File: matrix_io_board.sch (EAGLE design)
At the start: 114 parts, among them IC1 6N138, IC2 SN74LVC2G14, IC3 LM27675M5_CHARGEPUMP, IC4 LM324D, IC5 MCP4728_QUAD_DAC, IC6 4504D, IC7 SP34063A_BOOST_REG, IC8 FDS8958B

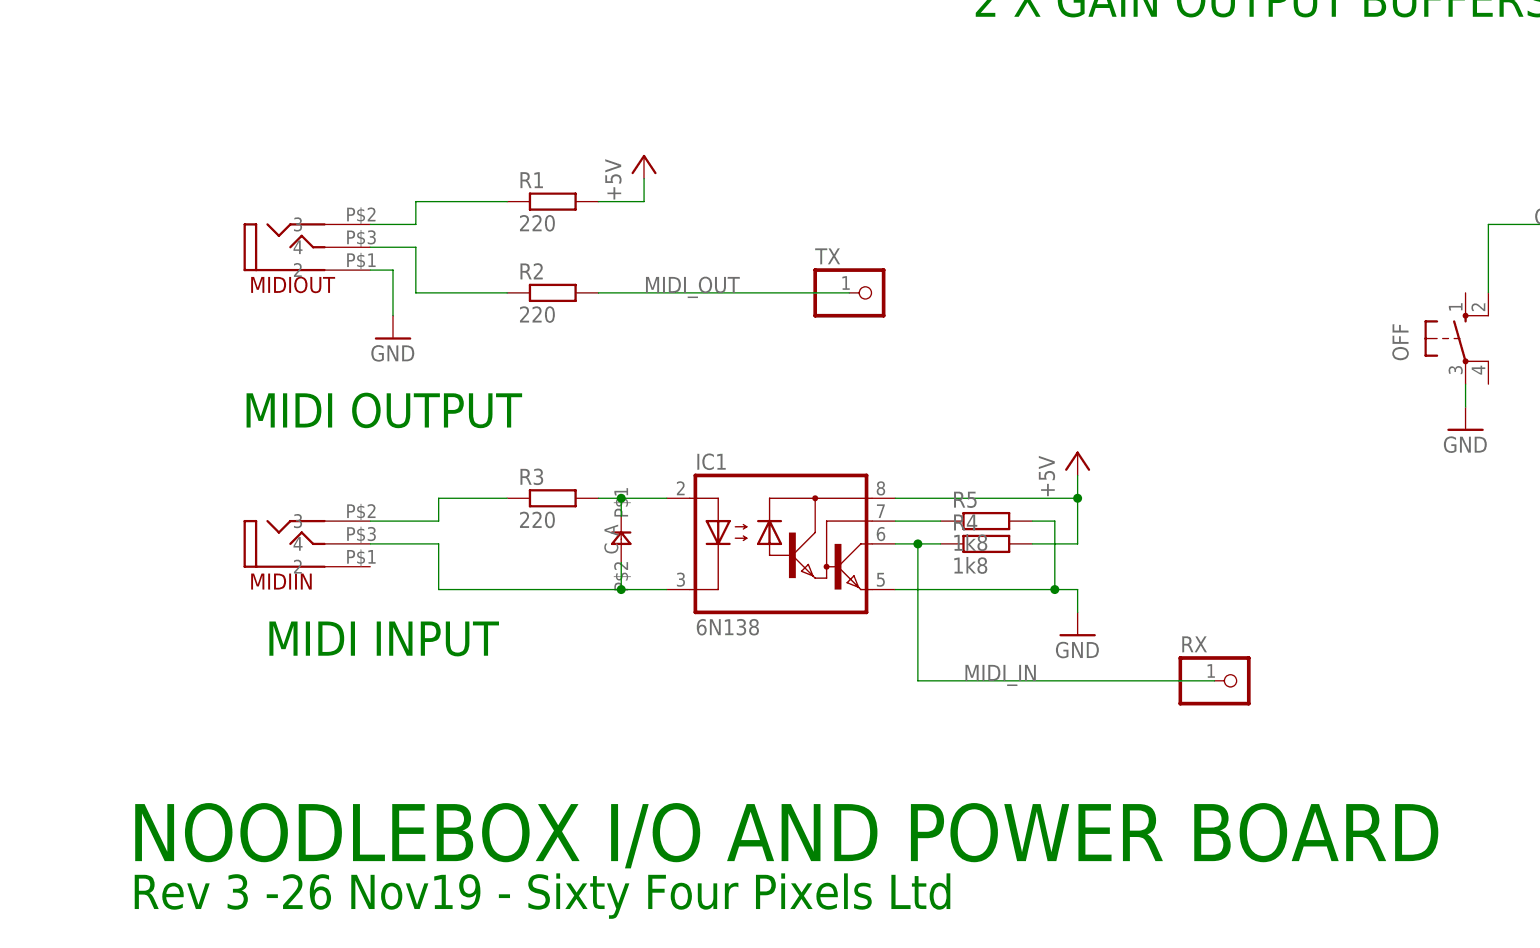
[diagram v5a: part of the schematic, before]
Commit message: use the new stereo Thonk sockets
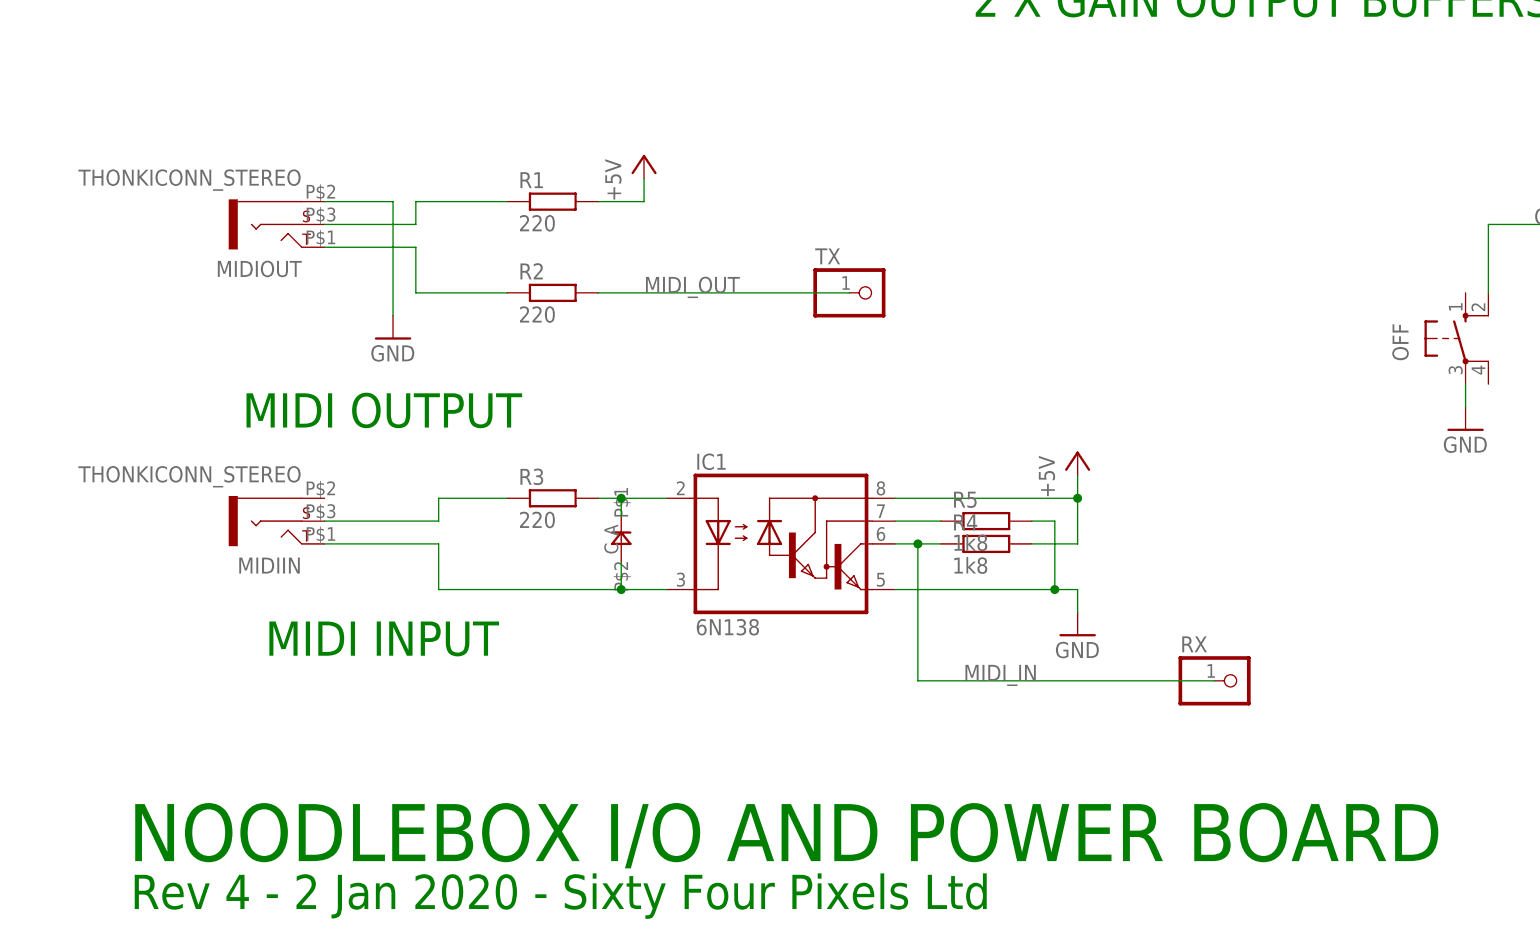
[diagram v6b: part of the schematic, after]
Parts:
- MIDIIN, MIDIOUT: value VERTICAL_3_5MM_SOCKETASSS -> THONKICONN_STEREO; device jason_eagle6:VERTICAL_3_5MM_SOCKETASSS -> jason_eagle6:THONKICONN_STEREO
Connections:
- net GND: now also MIDIOUT.R; no longer MIDIOUT.2
- net N$1: now also MIDIOUT.S; no longer MIDIOUT.3
- net N$4: now also MIDIIN.T; no longer MIDIIN.4
- net N$6: now also MIDIOUT.T; no longer MIDIOUT.4
- net N$7: now also MIDIIN.S; no longer MIDIIN.3
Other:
- note added: "Rev 4 - 2 Jan 2020 - Sixty Four Pixels Ltd"
- note removed: "Rev 3 -26 Nov19 - Sixty Four Pixels Ltd"
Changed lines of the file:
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@@
 <part name="C10" library="rcl" deviceset="C-EU" device="C0805" value="100n"/>
 <part name="GND29" library="supply1" deviceset="GND" device=""/>
-<part name="MIDIOUT" library="jason_eagle6" deviceset="VERTICAL_3_5MM_SOCKET" device="ASSS" value="VERTICAL_3_5MM_SOCKETASSS"/>
-<part name="MIDIIN" library="jason_eagle6" deviceset="VERTICAL_3_5MM_SOCKET" device="ASSS" value="VERTICAL_3_5MM_SOCKETASSS"/>
 <part name="CKO" library="thonkiconn" deviceset="WQP-PJ301M-12_JACK" device=""/>
 <part name="GT2" library="thonkiconn" deviceset="WQP-PJ301M-12_JACK" device=""/>
@@
 <part name="GD3" library="pinhead" deviceset="PINHD-1X1" device=""/>
 <part name="GD4" library="pinhead" deviceset="PINHD-1X1" device=""/>
+<part name="MIDIOUT" library="jason_eagle6" deviceset="THONKICONN_STEREO" device=""/>
+<part name="MIDIIN" library="jason_eagle6" deviceset="THONKICONN_STEREO" device=""/>
 </parts>
 <sheets>
@@
 <text x="359.156" y="117.094" size="3.81" layer="91">CLOCK INPUT</text>
 <text x="105.156" y="99.314" size="6.35" layer="91">NOODLEBOX I/O AND POWER BOARD</text>
-<text x="105.41" y="93.98" size="3.81" layer="91">Rev 3 -26 Nov19 - Sixty Four Pixels Ltd</text>
+<text x="105.41" y="93.98" size="3.81" layer="91">Rev 4 - 2 Jan 2020 - Sixty Four Pixels Ltd</text>
 </plain>
 <instances>
@@
 <instance part="C10" gate="G$1" x="416.56" y="228.6" rot="R180"/>
 <instance part="GND29" gate="1" x="396.24" y="215.9"/>
-<instance part="MIDIOUT" gate="G$1" x="121.92" y="167.64" rot="MR180"/>
-<instance part="MIDIIN" gate="G$1" x="121.92" y="134.62" rot="MR180"/>
 <instance part="CKO" gate="G$1" x="444.5" y="251.46" rot="MR180"/>
 <instance part="GT2" gate="G$1" x="444.5" y="241.3" rot="MR180"/>
@@
 <instance part="GD3" gate="G$1" x="429.26" y="327.66"/>
 <instance part="GD4" gate="G$1" x="429.26" y="320.04"/>
+<instance part="MIDIOUT" gate="G$1" x="121.92" y="170.18" rot="R180"/>
+<instance part="MIDIIN" gate="G$1" x="121.92" y="137.16" rot="R180"/>
 </instances>
 <busses>
@@
 <wire x1="160.02" y1="132.588" x2="160.02" y2="129.54" width="0.1524" layer="91"/>
 <junction x="160.02" y="129.54"/>
-<pinref part="MIDIIN" gate="G$1" pin="4"/>
-<wire x1="132.08" y1="134.62" x2="139.7" y2="134.62" width="0.1524" layer="91"/>
 <wire x1="139.7" y1="134.62" x2="139.7" y2="129.54" width="0.1524" layer="91"/>
+<pinref part="MIDIIN" gate="G$1" pin="T"/>
+<wire x1="127" y1="134.62" x2="139.7" y2="134.62" width="0.1524" layer="91"/>
 </segment>
 </net>
@@
 </segment>
 <segment>
-<pinref part="MIDIOUT" gate="G$1" pin="2"/>
 <pinref part="GND40" gate="1" pin="GND"/>
-<wire x1="132.08" y1="165.1" x2="134.62" y2="165.1" width="0.1524" layer="91"/>
-<wire x1="134.62" y1="165.1" x2="134.62" y2="160.02" width="0.1524" layer="91"/>
+<pinref part="MIDIOUT" gate="G$1" pin="R"/>
+<wire x1="127" y1="172.72" x2="134.62" y2="172.72" width="0.1524" layer="91"/>
+<wire x1="134.62" y1="172.72" x2="134.62" y2="160.02" width="0.1524" layer="91"/>
 </segment>
 </net>
@@
 <wire x1="137.16" y1="162.56" x2="147.32" y2="162.56" width="0.1524" layer="91"/>
 <wire x1="137.16" y1="162.56" x2="137.16" y2="167.64" width="0.1524" layer="91"/>
-<pinref part="MIDIOUT" gate="G$1" pin="4"/>
-<wire x1="137.16" y1="167.64" x2="132.08" y2="167.64" width="0.1524" layer="91"/>
+<wire x1="137.16" y1="167.64" x2="127" y2="167.64" width="0.1524" layer="91"/>
+<pinref part="MIDIOUT" gate="G$1" pin="T"/>
 </segment>
 </net>
@@
 <wire x1="147.32" y1="139.7" x2="139.7" y2="139.7" width="0.1524" layer="91"/>
 <wire x1="139.7" y1="139.7" x2="139.7" y2="137.16" width="0.1524" layer="91"/>
-<pinref part="MIDIIN" gate="G$1" pin="3"/>
-<wire x1="139.7" y1="137.16" x2="132.08" y2="137.16" width="0.1524" layer="91"/>
+<pinref part="MIDIIN" gate="G$1" pin="S"/>
+<wire x1="127" y1="137.16" x2="139.7" y2="137.16" width="0.1524" layer="91"/>
 </segment>
 </net>
@@
 <segment>
 <pinref part="R1" gate="G$1" pin="1"/>
-<pinref part="MIDIOUT" gate="G$1" pin="3"/>
-<wire x1="132.08" y1="170.18" x2="137.16" y2="170.18" width="0.1524" layer="91"/>
+<wire x1="127" y1="170.18" x2="137.16" y2="170.18" width="0.1524" layer="91"/>
 <wire x1="137.16" y1="170.18" x2="137.16" y2="172.72" width="0.1524" layer="91"/>
 <wire x1="137.16" y1="172.72" x2="147.32" y2="172.72" width="0.1524" layer="91"/>
-</segment>
-</net>
+<pinref part="MIDIOUT" gate="G$1" pin="S"/>
+</segment>
+</net>

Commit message: V4 ready to go
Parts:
- renumbered BATT+ to BT+, BATT- to BT-
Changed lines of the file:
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@@
 <part name="GND41" library="supply1" deviceset="GND" device=""/>
 <part name="L2" library="jason_eagle6" deviceset="NB_IND" device=""/>
-<part name="BATT+" library="pinhead" deviceset="PINHD-1X1" device=""/>
-<part name="BATT-" library="pinhead" deviceset="PINHD-1X1" device=""/>
+<part name="BT+" library="pinhead" deviceset="PINHD-1X1" device=""/>
+<part name="BT-" library="pinhead" deviceset="PINHD-1X1" device=""/>
 <part name="C1" library="rcl" deviceset="C-EU" device="C0805" value="100n"/>
 <part name="P+13" library="supply1" deviceset="+5V" device=""/>
@@
 <instance part="GND41" gate="1" x="284.48" y="299.72"/>
 <instance part="L2" gate="G$1" x="259.08" y="330.2" rot="R90"/>
-<instance part="BATT+" gate="G$1" x="99.06" y="368.3" rot="R180"/>
-<instance part="BATT-" gate="G$1" x="99.06" y="360.68" rot="R180"/>
+<instance part="BT+" gate="G$1" x="99.06" y="368.3" rot="R180"/>
+<instance part="BT-" gate="G$1" x="99.06" y="360.68" rot="R180"/>
 <instance part="C1" gate="G$1" x="335.28" y="147.32"/>
 <instance part="P+13" gate="1" x="335.28" y="170.18"/>
@@
 <wire x1="109.22" y1="347.98" x2="111.76" y2="347.98" width="0.1524" layer="91"/>
 <wire x1="111.76" y1="347.98" x2="111.76" y2="340.36" width="0.1524" layer="91"/>
-<pinref part="BATT-" gate="G$1" pin="1"/>
+<pinref part="BT-" gate="G$1" pin="1"/>
 <wire x1="101.6" y1="360.68" x2="111.76" y2="360.68" width="0.1524" layer="91"/>
 <wire x1="111.76" y1="347.98" x2="111.76" y2="360.68" width="0.1524" layer="91"/>
@@
 <net name="N$16" class="0">
 <segment>
-<pinref part="BATT+" gate="G$1" pin="1"/>
+<pinref part="BT+" gate="G$1" pin="1"/>
 <wire x1="101.6" y1="368.3" x2="114.3" y2="368.3" width="0.1524" layer="91"/>
 <pinref part="DC" gate="G$1" pin="NC"/>

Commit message: V5 first cut
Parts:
- C10, C11, C12, C5, C6, C7: value 100n -> 10n
- C19, C20, C22: device rcl:CPOL-EUE2.5-7 -> rcl:CPOL-EUD
- D7: value CGRM4001-G -> MBR0520LT; device diode:CGRM4001-G -> diode:MBR0520LT
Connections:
- net GND: now also MIDIOUT.S; no longer MIDIOUT.R
- net N$1: now also MIDIOUT.R; no longer MIDIOUT.S
- net N$7: now also MIDIIN.R; no longer MIDIIN.S
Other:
- note added: "CC-NC-BY-SA Commercial Use Not Allowed"
- note added: "Rev 5 - 18 Feb 2020 - Sixty Four Pixels Ltd"
- note removed: "Rev 4 - 2 Jan 2020 - Sixty Four Pixels Ltd"
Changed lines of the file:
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@@
 <part name="R29" library="rcl" deviceset="R-EU_" device="R0805" value="0r33"/>
 <part name="GND7" library="supply1" deviceset="GND" device=""/>
-<part name="C22" library="rcl" deviceset="CPOL-EU" device="E2.5-7"/>
+<part name="C22" library="rcl" deviceset="CPOL-EU" device="D"/>
 <part name="GND8" library="supply1" deviceset="GND" device=""/>
 <part name="R30" library="rcl" deviceset="R-EU_" device="R0805" value="1k"/>
@@
 <part name="C21" library="rcl" deviceset="C-EU" device="C0805" value="470p"/>
 <part name="GND9" library="supply1" deviceset="GND" device=""/>
-<part name="D7" library="diode" deviceset="CGRM400*-G" device="" technology="1"/>
 <part name="GND10" library="supply1" deviceset="GND" device=""/>
-<part name="C20" library="rcl" deviceset="CPOL-EU" device="E2.5-7"/>
+<part name="C20" library="rcl" deviceset="CPOL-EU" device="D"/>
 <part name="GND11" library="supply1" deviceset="GND" device=""/>
 <part name="P+6" library="supply1" deviceset="+5V" device=""/>
@@
 <part name="GND40" library="supply1" deviceset="GND" device=""/>
 <part name="L1" library="SparkFun" deviceset="INDUCTOR" device="1210"/>
-<part name="C19" library="rcl" deviceset="CPOL-EU" device="E2.5-7"/>
+<part name="C19" library="rcl" deviceset="CPOL-EU" device="D"/>
 <part name="GND41" library="supply1" deviceset="GND" device=""/>
 <part name="L2" library="jason_eagle6" deviceset="NB_IND" device=""/>
@@
 <part name="R6" library="rcl" deviceset="R-EU_" device="R0805" value="100k"/>
 <part name="GND26" library="supply1" deviceset="GND" device=""/>
-<part name="C5" library="rcl" deviceset="C-EU" device="C0805" value="100n"/>
-<part name="C6" library="rcl" deviceset="C-EU" device="C0805" value="100n"/>
-<part name="C7" library="rcl" deviceset="C-EU" device="C0805" value="100n"/>
-<part name="C11" library="rcl" deviceset="C-EU" device="C0805" value="100n"/>
-<part name="C10" library="rcl" deviceset="C-EU" device="C0805" value="100n"/>
+<part name="C5" library="rcl" deviceset="C-EU" device="C0805" value="10n"/>
+<part name="C6" library="rcl" deviceset="C-EU" device="C0805" value="10n"/>
+<part name="C7" library="rcl" deviceset="C-EU" device="C0805" value="10n"/>
+<part name="C11" library="rcl" deviceset="C-EU" device="C0805" value="10n"/>
+<part name="C10" library="rcl" deviceset="C-EU" device="C0805" value="10n"/>
 <part name="GND29" library="supply1" deviceset="GND" device=""/>
 <part name="CKO" library="thonkiconn" deviceset="WQP-PJ301M-12_JACK" device=""/>
@@
 <part name="AUXI" library="thonkiconn" deviceset="WQP-PJ301M-12_JACK" device=""/>
 <part name="R15" library="rcl" deviceset="R-EU_" device="R0805" value="1k"/>
-<part name="C12" library="rcl" deviceset="C-EU" device="C0805" value="100n"/>
+<part name="C12" library="rcl" deviceset="C-EU" device="C0805" value="10n"/>
 <part name="IC2" library="jason_eagle6" deviceset="SN74LVC2G14" device=""/>
 <part name="R9" library="rcl" deviceset="R-EU_" device="R0805" value="1k"/>
@@
 <part name="MIDIOUT" library="jason_eagle6" deviceset="THONKICONN_STEREO" device=""/>
 <part name="MIDIIN" library="jason_eagle6" deviceset="THONKICONN_STEREO" device=""/>
+<part name="D7" library="diode" deviceset="MBR0520LT" device=""/>
 </parts>
 <sheets>
@@
 <text x="359.156" y="117.094" size="3.81" layer="91">CLOCK INPUT</text>
 <text x="105.156" y="99.314" size="6.35" layer="91">NOODLEBOX I/O AND POWER BOARD</text>
-<text x="105.41" y="93.98" size="3.81" layer="91">Rev 4 - 2 Jan 2020 - Sixty Four Pixels Ltd</text>
+<text x="105.41" y="93.98" size="3.81" layer="91">Rev 5 - 18 Feb 2020 - Sixty Four Pixels Ltd</text>
+<text x="105.41" y="88.9" size="3.81" layer="91">CC-NC-BY-SA Commercial Use Not Allowed</text>
 </plain>
 <instances>
@@
 <instance part="C21" gate="G$1" x="241.3" y="332.74"/>
 <instance part="GND9" gate="1" x="241.3" y="322.58"/>
-<instance part="D7" gate="G$1" x="246.38" y="330.2" rot="R90"/>
 <instance part="GND10" gate="1" x="246.38" y="322.58"/>
 <instance part="C20" gate="G$1" x="259.08" y="309.88"/>
@@
 <instance part="MIDIOUT" gate="G$1" x="121.92" y="170.18" rot="R180"/>
 <instance part="MIDIIN" gate="G$1" x="121.92" y="137.16" rot="R180"/>
+<instance part="D7" gate="G$1" x="246.38" y="330.2" rot="R90"/>
 </instances>
 <busses>
@@
 <segment>
 <pinref part="GND10" gate="1" pin="GND"/>
+<wire x1="246.38" y1="325.12" x2="246.38" y2="327.66" width="0.1524" layer="91"/>
 <pinref part="D7" gate="G$1" pin="A"/>
-<wire x1="246.38" y1="325.12" x2="246.38" y2="327.66" width="0.1524" layer="91"/>
 </segment>
 <segment>
@@
 <segment>
 <pinref part="GND40" gate="1" pin="GND"/>
-<pinref part="MIDIOUT" gate="G$1" pin="R"/>
+<wire x1="134.62" y1="172.72" x2="134.62" y2="160.02" width="0.1524" layer="91"/>
+<pinref part="MIDIOUT" gate="G$1" pin="S"/>
 <wire x1="127" y1="172.72" x2="134.62" y2="172.72" width="0.1524" layer="91"/>
-<wire x1="134.62" y1="172.72" x2="134.62" y2="160.02" width="0.1524" layer="91"/>
 </segment>
 </net>
@@
 <segment>
 <pinref part="IC7" gate="G$1" pin="SW_E"/>
-<pinref part="D7" gate="G$1" pin="C"/>
 <wire x1="233.68" y1="340.36" x2="246.38" y2="340.36" width="0.1524" layer="91"/>
 <wire x1="246.38" y1="340.36" x2="246.38" y2="332.74" width="0.1524" layer="91"/>
@@
 <pinref part="L2" gate="G$1" pin="2"/>
 <wire x1="259.08" y1="335.28" x2="259.08" y2="340.36" width="0.1524" layer="91"/>
+<pinref part="D7" gate="G$1" pin="C"/>
 </segment>
 </net>
@@
 <segment>
 <pinref part="R3" gate="G$1" pin="1"/>
-<wire x1="147.32" y1="139.7" x2="139.7" y2="139.7" width="0.1524" layer="91"/>
-<wire x1="139.7" y1="139.7" x2="139.7" y2="137.16" width="0.1524" layer="91"/>
-<pinref part="MIDIIN" gate="G$1" pin="S"/>
+<pinref part="MIDIIN" gate="G$1" pin="R"/>
+<wire x1="139.7" y1="139.7" x2="147.32" y2="139.7" width="0.1524" layer="91"/>
 <wire x1="127" y1="137.16" x2="139.7" y2="137.16" width="0.1524" layer="91"/>
+<wire x1="139.7" y1="137.16" x2="139.7" y2="139.7" width="0.1524" layer="91"/>
 </segment>
 </net>
@@
 <segment>
 <pinref part="R1" gate="G$1" pin="1"/>
-<wire x1="127" y1="170.18" x2="137.16" y2="170.18" width="0.1524" layer="91"/>
 <wire x1="137.16" y1="170.18" x2="137.16" y2="172.72" width="0.1524" layer="91"/>
 <wire x1="137.16" y1="172.72" x2="147.32" y2="172.72" width="0.1524" layer="91"/>
-<pinref part="MIDIOUT" gate="G$1" pin="S"/>
-</segment>
-</net>
+<pinref part="MIDIOUT" gate="G$1" pin="R"/>
+<wire x1="127" y1="170.18" x2="137.16" y2="170.18" width="0.1524" layer="91"/>
+</segment>
+</net>
